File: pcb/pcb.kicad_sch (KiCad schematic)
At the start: 14 parts, among them J1 L_motors, J2 R_motors, M0 Motor_DC, M1 Motor_DC, M2 Motor_DC, M3 Motor_DC, U0 ATmega328-P, U1 DRV8800PWP, U2 DRV8800PWP

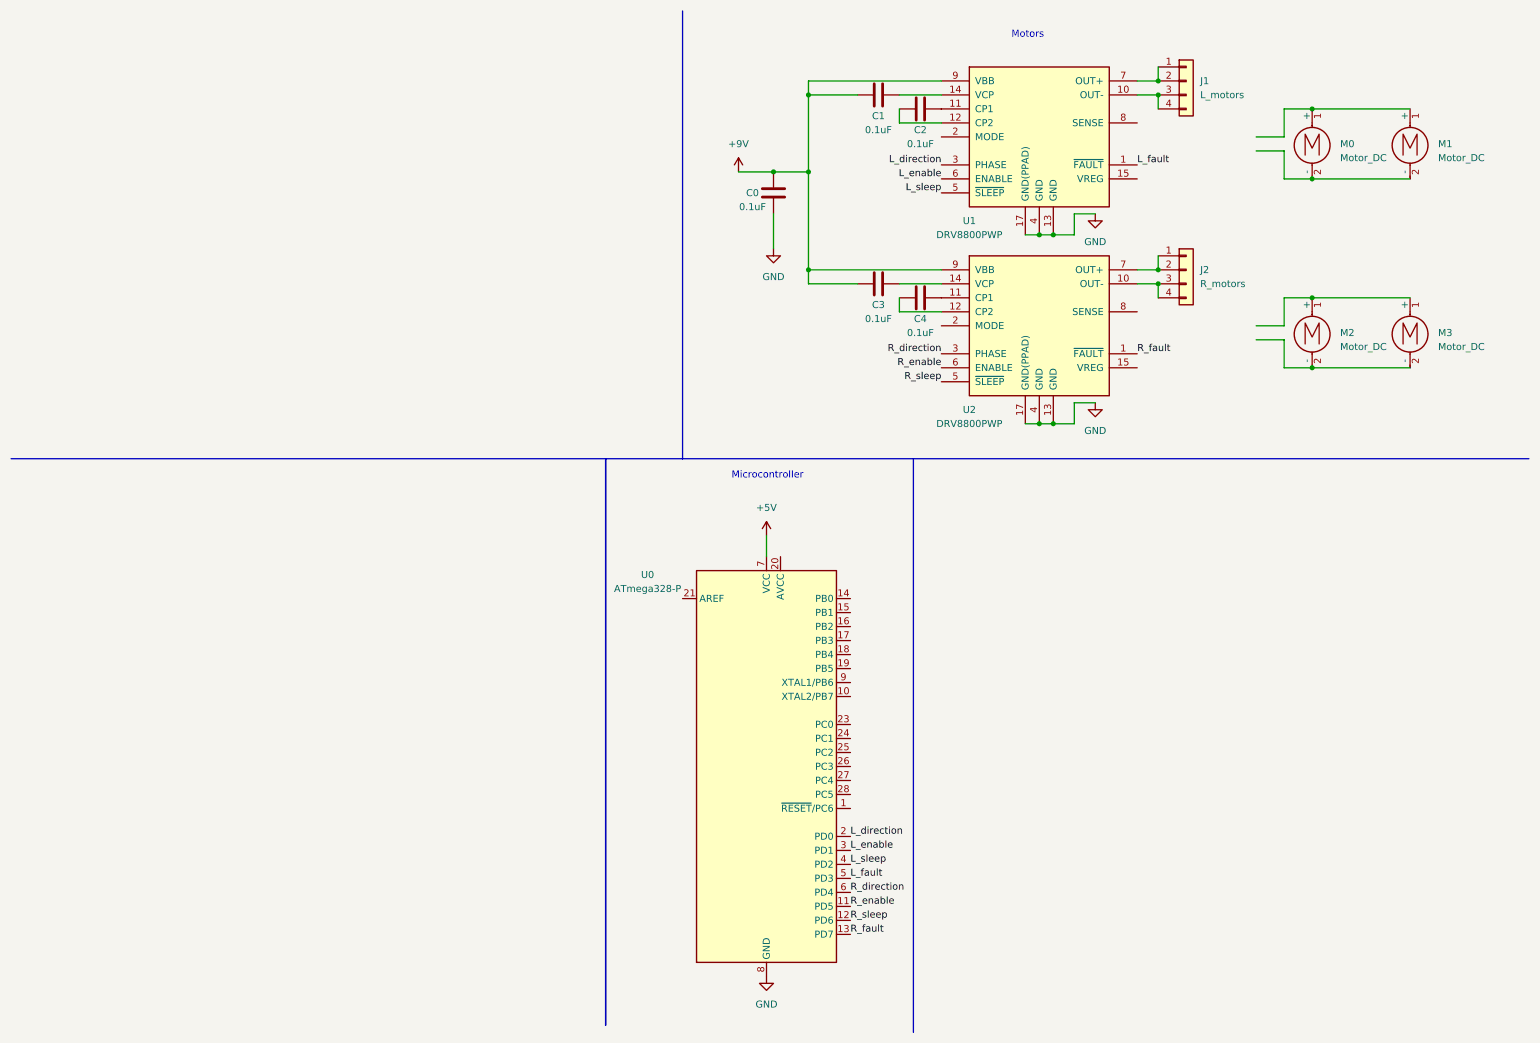
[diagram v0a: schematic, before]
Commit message: Added more details to the schematic
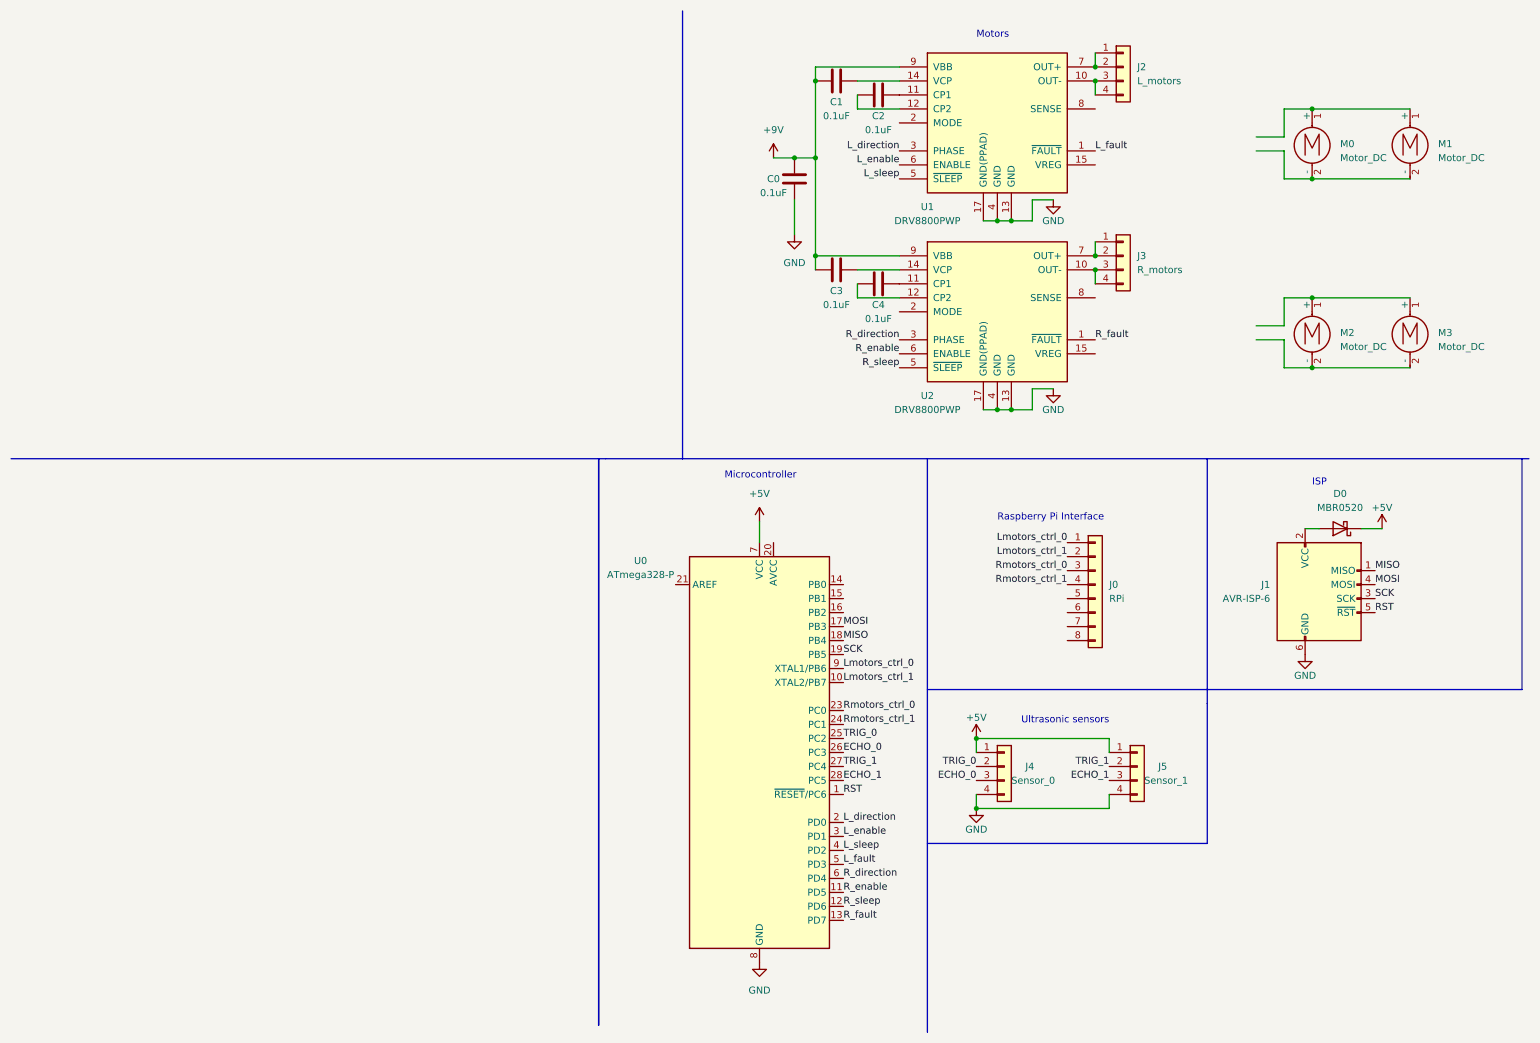
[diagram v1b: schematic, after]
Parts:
- added D0: MBR0520, Diode_SMD:D_SOD-123, symbol Diode:MBR0520
- added J0: RPi, symbol Connector_Generic:Conn_01x08
- added J1: AVR-ISP-6, symbol Connector:AVR-ISP-6
- added J4: Sensor_0, symbol Connector_Generic:Conn_01x04
- added J5: Sensor_1, symbol Connector_Generic:Conn_01x04
- renumbered J1 to J2, J2 to J3
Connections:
- net +5V: now also D0.1 (K), J4.1 (Pin_1), J5.1 (Pin_1)
- net GND: now also J1.6 (GND), J4.4 (Pin_4), J5.4 (Pin_4)
- net RST: now reaches U0.1 (~{RESET}/PC6)
- net RST: now also J1.5 (~{RST})
- net Lmotors_ctrl_1: now reaches U0.10 (XTAL2/PB7)
- net Lmotors_ctrl_1: now also J0.2 (Pin_2)
- net MOSI: now reaches U0.17 (PB3)
- net MOSI: now also J1.4 (MOSI)
- net MISO: now reaches U0.18 (PB4)
- net MISO: now also J1.1 (MISO)
- net SCK: now reaches U0.19 (PB5)
- net SCK: now also J1.3 (SCK)
- net Rmotors_ctrl_0: now reaches U0.23 (PC0)
- net Rmotors_ctrl_0: now also J0.3 (Pin_3)
- net Rmotors_ctrl_1: now reaches U0.24 (PC1)
- net Rmotors_ctrl_1: now also J0.4 (Pin_4)
- net TRIG_0: now reaches U0.25 (PC2)
- net TRIG_0: now also J4.2 (Pin_2)
- net ECHO_0: now reaches U0.26 (PC3)
- net ECHO_0: now also J4.3 (Pin_3)
- net TRIG_1: now reaches U0.27 (PC4)
- net TRIG_1: now also J5.2 (Pin_2)
- net ECHO_1: now reaches U0.28 (PC5)
- net ECHO_1: now also J5.3 (Pin_3)
- net Lmotors_ctrl_0: now reaches U0.9 (XTAL1/PB6)
- net Lmotors_ctrl_0: now also J0.1 (Pin_1)
- new net: D0.2 (A), J1.2 (VCC)
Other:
- note added: "ISP"
- note added: "Raspberry Pi Interface"
- note added: "Ultrasonic sensors"
- moved on the sheet: C0, C1, C2, C3, C4, J2, J3, U0, U1, U2
